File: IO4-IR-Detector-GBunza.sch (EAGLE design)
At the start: 51 parts, among them CON2 IO4INV, Q1 2N7002, Q2 2N7002, Q3 2N7002, Q4 2N7002, U1 LM358B, U2 LM393M

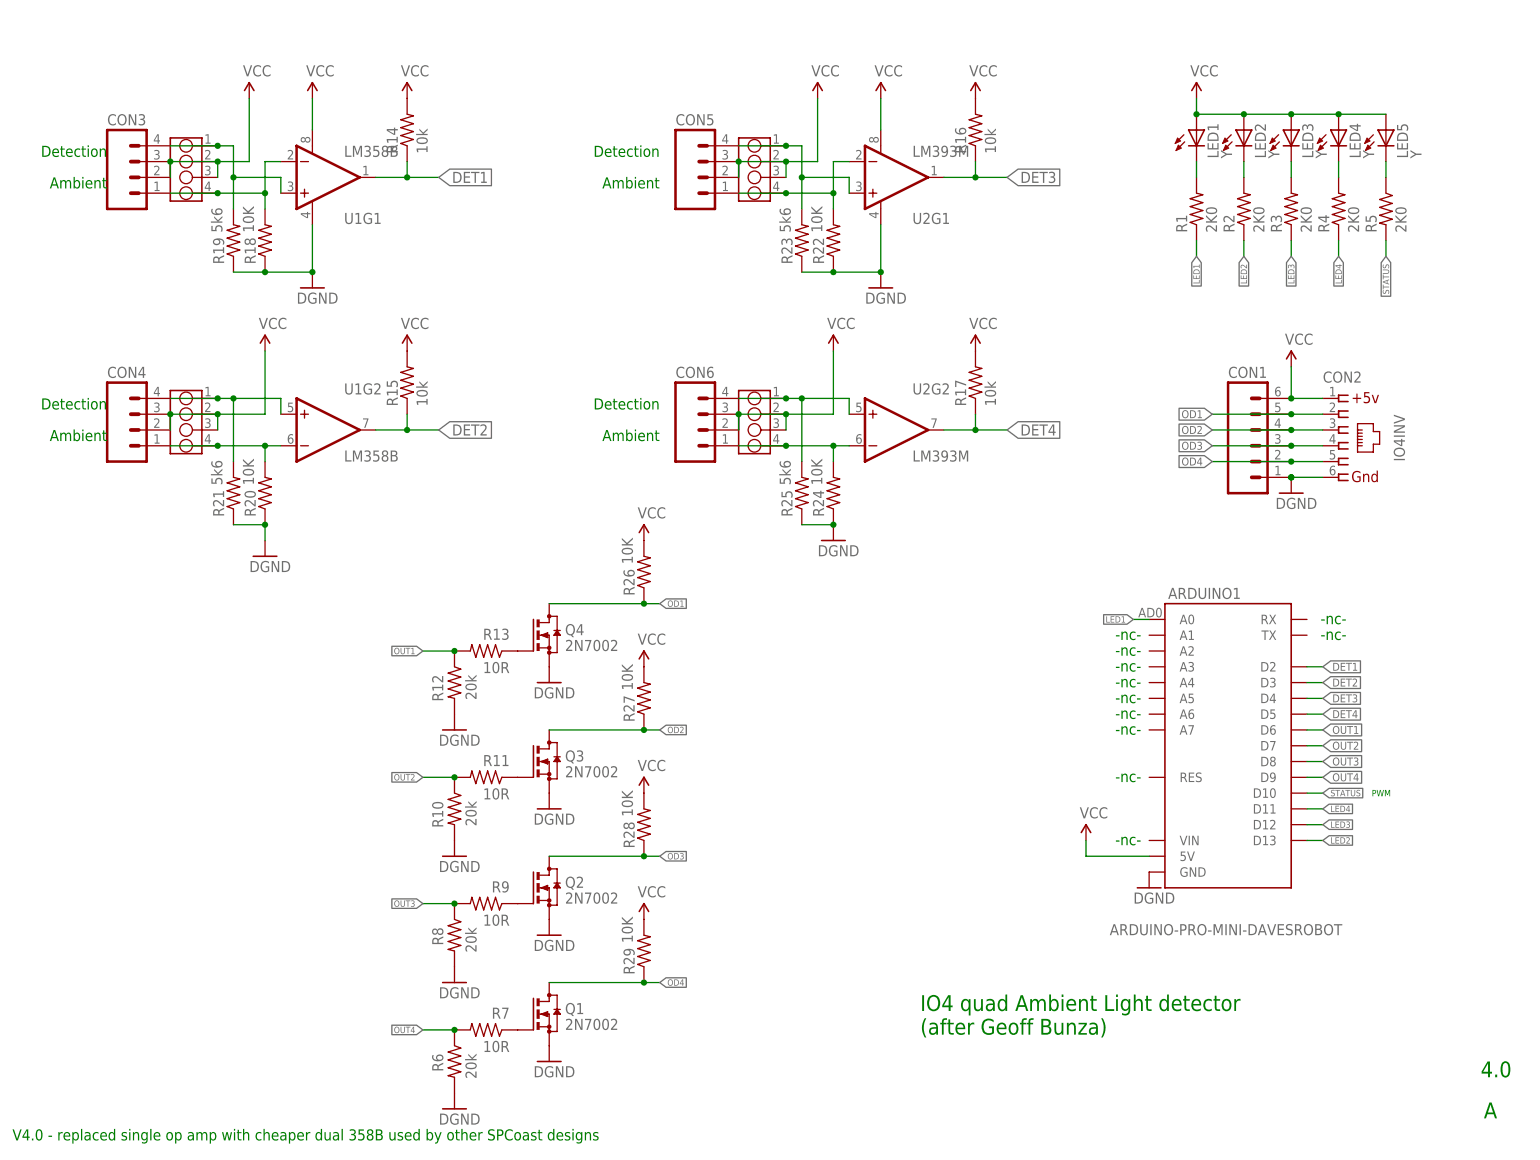
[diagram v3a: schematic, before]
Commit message: normalized values
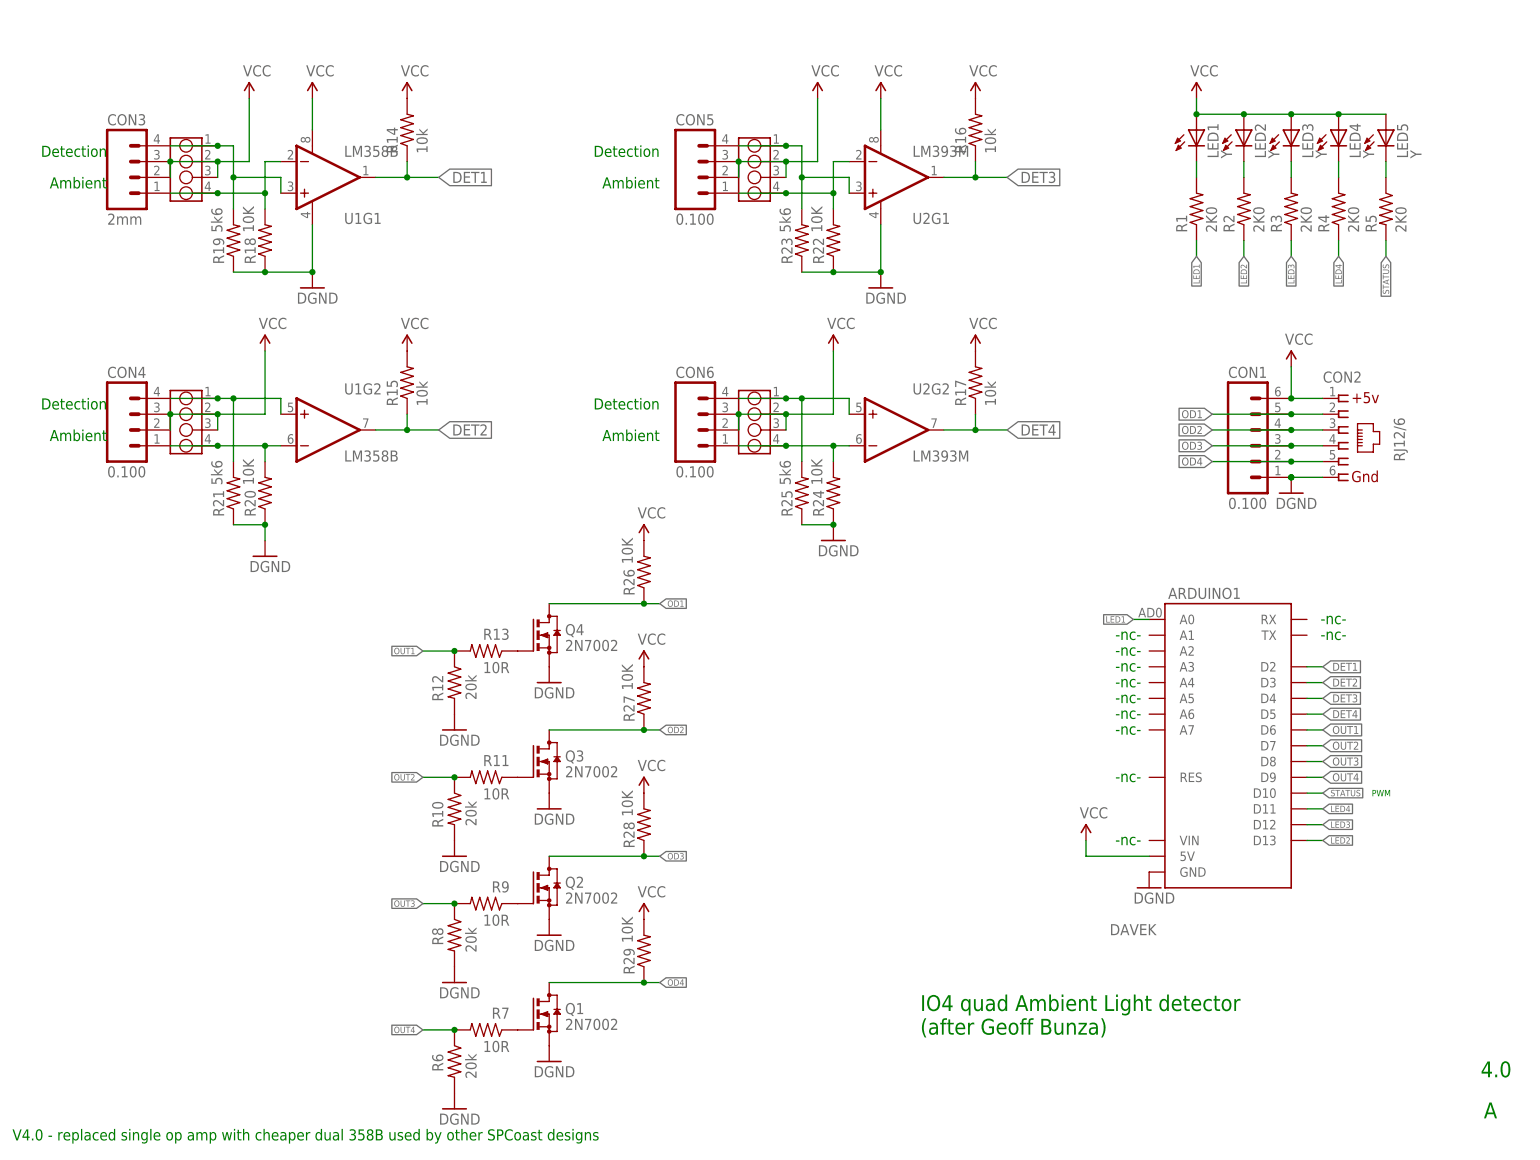
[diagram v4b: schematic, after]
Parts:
- ARDUINO1: value ARDUINO-PRO-MINI-DAVESROBOT -> DAVEK
- CON1, CON4, CON5, CON6: value (none) -> 0.100
- CON2: value IO4INV -> RJ12/6
- CON3: value (none) -> 2mm
- DET1, DET2, DET3, DET4: value CONNECTOR-GROVE-4P-2.0-3470130P1 -> 2mm
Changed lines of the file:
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@@
 <part name="R19" library="SPCoast" deviceset="R*" device="0805-RES" value="5k6"/>
 <part name="R14" library="SPCoast" deviceset="R*" device="0805-RES" value="10k"/>
-<part name="CON2" library="SPCoast" deviceset="CONNECTOR-IO4" device="INV" value="IO4INV"/>
+<part name="CON2" library="SPCoast" deviceset="CONNECTOR-IO4" device="INV" value="RJ12/6"/>
 <part name="GND5" library="SparkFun-Aesthetics" deviceset="DGND" device=""/>
 <part name="SUPPLY5" library="SparkFun-Aesthetics" deviceset="VCC" device=""/>
-<part name="ARDUINO1" library="SPCoast" deviceset="ARDUINO-PRO-MINI" device="DAVESROBOT" value="ARDUINO-PRO-MINI-DAVESROBOT"/>
+<part name="ARDUINO1" library="SPCoast" deviceset="ARDUINO-PRO-MINI" device="DAVESROBOT" value="DAVEK"/>
 <part name="SUPPLY7" library="SparkFun-Aesthetics" deviceset="VCC" device=""/>
 <part name="GND7" library="SparkFun-Aesthetics" deviceset="DGND" device=""/>
@@
 <part name="R2" library="SPCoast" deviceset="R*" device="0805-RES" value="2K0"/>
 <part name="R1" library="SPCoast" deviceset="R*" device="0805-RES" value="2K0"/>
-<part name="CON1" library="SPCoast" deviceset="CONNECTOR-M06" device="LOCK"/>
+<part name="CON1" library="SPCoast" deviceset="CONNECTOR-M06" device="LOCK" value="0.100"/>
 <part name="GND13" library="SparkFun-Aesthetics" deviceset="DGND" device=""/>
 <part name="SUPPLY4" library="SparkFun-Aesthetics" deviceset="VCC" device=""/>
-<part name="DET1" library="SPCoast" deviceset="CONNECTOR-GROVE-4P-2.0" device="-3470130P1"/>
+<part name="DET1" library="SPCoast" deviceset="CONNECTOR-GROVE-4P-2.0" device="-3470130P1" value="2mm"/>
 <part name="R20" library="SPCoast" deviceset="R*" device="0805-RES" value="10K"/>
 <part name="R21" library="SPCoast" deviceset="R*" device="0805-RES" value="5k6"/>
 <part name="R15" library="SPCoast" deviceset="R*" device="0805-RES" value="10k"/>
 <part name="GND1" library="SparkFun-Aesthetics" deviceset="DGND" device=""/>
-<part name="DET2" library="SPCoast" deviceset="CONNECTOR-GROVE-4P-2.0" device="-3470130P1"/>
+<part name="DET2" library="SPCoast" deviceset="CONNECTOR-GROVE-4P-2.0" device="-3470130P1" value="2mm"/>
 <part name="R22" library="SPCoast" deviceset="R*" device="0805-RES" value="10K"/>
 <part name="R23" library="SPCoast" deviceset="R*" device="0805-RES" value="5k6"/>
@@
 <part name="GND2" library="SparkFun-Aesthetics" deviceset="DGND" device=""/>
 <part name="SUPPLY2" library="SparkFun-Aesthetics" deviceset="VCC" device=""/>
-<part name="DET3" library="SPCoast" deviceset="CONNECTOR-GROVE-4P-2.0" device="-3470130P1"/>
+<part name="DET3" library="SPCoast" deviceset="CONNECTOR-GROVE-4P-2.0" device="-3470130P1" value="2mm"/>
 <part name="R24" library="SPCoast" deviceset="R*" device="0805-RES" value="10K"/>
 <part name="R25" library="SPCoast" deviceset="R*" device="0805-RES" value="5k6"/>
 <part name="R17" library="SPCoast" deviceset="R*" device="0805-RES" value="10k"/>
-<part name="DET4" library="SPCoast" deviceset="CONNECTOR-GROVE-4P-2.0" device="-3470130P1"/>
+<part name="DET4" library="SPCoast" deviceset="CONNECTOR-GROVE-4P-2.0" device="-3470130P1" value="2mm"/>
 <part name="LED5" library="SPCoast" deviceset="LED*" device="0603-LED" value="Y"/>
 <part name="R5" library="SPCoast" deviceset="R*" device="0805-RES" value="2K0"/>
@@
 <part name="SUPPLY16" library="SparkFun-Aesthetics" deviceset="VCC" device=""/>
 <part name="SUPPLY17" library="SparkFun-Aesthetics" deviceset="VCC" device=""/>
-<part name="CON3" library="SPCoast" deviceset="CONNECTOR-M04" device="LOCK"/>
-<part name="CON4" library="SPCoast" deviceset="CONNECTOR-M04" device="LOCK"/>
-<part name="CON5" library="SPCoast" deviceset="CONNECTOR-M04" device="LOCK"/>
-<part name="CON6" library="SPCoast" deviceset="CONNECTOR-M04" device="LOCK"/>
+<part name="CON3" library="SPCoast" deviceset="CONNECTOR-M04" device="LOCK" value="2mm"/>
+<part name="CON4" library="SPCoast" deviceset="CONNECTOR-M04" device="LOCK" value="0.100"/>
+<part name="CON5" library="SPCoast" deviceset="CONNECTOR-M04" device="LOCK" value="0.100"/>
+<part name="CON6" library="SPCoast" deviceset="CONNECTOR-M04" device="LOCK" value="0.100"/>
 </parts>
 <sheets>

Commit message: Vscore changed to mouse bites, larger
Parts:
- R1, R10, R11, R12, R13, R14, R15, R16, R17, R18, R19, R2, R20, R21, R22, R23, R24, R25, R26, R27, R28, R29, R3, R4, R5, R6, R7, R8, R9: device SPCoast:R0805-RES -> SPCoast:R0603-RES
